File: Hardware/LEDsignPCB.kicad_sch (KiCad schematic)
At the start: 0 parts

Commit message: PD chip and usbc receptacle
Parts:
- added J?: USB_C_Receptacle, symbol Connector:USB_C_Receptacle
- added U?: CH224K, Package_SO:SSOP-10-1EP_3.9x4.9mm_P1mm_EP2.1x3.3mm, symbol Interface_USB:CH224K
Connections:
- new net: J?.A1 (GND), J?.A12 (GND), J?.B1 (GND), J?.B12 (GND)
- new net: J?.A4 (VBUS), J?.A9 (VBUS), J?.B4 (VBUS), J?.B9 (VBUS)
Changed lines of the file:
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@@
 	(generator_version "9.0")
 	(paper "A4")
+	(symbol
+		(lib_id "Connector:USB_C_Receptacle")
+		(at 50.8 60.96 0)
+		(unit 1)
+		(exclude_from_sim no)
+		(in_bom yes)
+		(on_board yes)
+		(dnp no)
+		(fields_autoplaced yes)
+		(property "Reference" "J?"
+			(at 50.8 27.94 0)
+			(effects
+				(font
+					(size 1.27 1.27)
+				)
+			)
+		)
+		(property "Value" "USB_C_Receptacle"
+			(at 50.8 30.48 0)
+			(effects
+				(font
+					(size 1.27 1.27)
+				)
+			)
+		)
+		(property "Footprint" ""
+			(at 54.61 60.96 0)
+			(effects
+				(font
+					(size 1.27 1.27)
+				)
+				(hide yes)
+			)
+		)
+		(property "Datasheet" "https://www.usb.org/sites/default/files/documents/usb_type-c.zip"
+			(at 54.61 60.96 0)
+			(effects
+				(font
+					(size 1.27 1.27)
+				)
+				(hide yes)
+			)
+		)
+		(property "Description" "USB Full-Featured Type-C Receptacle connector"
+			(at 50.8 60.96 0)
+			(effects
+				(font
+					(size 1.27 1.27)
+				)
+				(hide yes)
+			)
+		)
+		(pin "S1"
+		)
+		(pin "B2"
+		)
+		(pin "A8"
+		)
+		(pin "A10"
+		)
+		(pin "A11"
+		)
+		(pin "B3"
+		)
+		(pin "A1"
+		)
+		(pin "A12"
+		)
+		(pin "B1"
+		)
+		(pin "B12"
+		)
+		(pin "A4"
+		)
+		(pin "A9"
+		)
+		(pin "B4"
+		)
+		(pin "B9"
+		)
+		(pin "A5"
+		)
+		(pin "B5"
+		)
+		(pin "A7"
+		)
+		(pin "B7"
+		)
+		(pin "A6"
+		)
+		(pin "B6"
+		)
+		(pin "B10"
+		)
+		(pin "B11"
+		)
+		(pin "A3"
+		)
+		(pin "A2"
+		)
+		(pin "B8"
+		)
+		(instances
+			(project ""
+				(path "/bd70e714-05b6-457c-88d3-c29e19a48f7d"
+					(reference "J?")
+					(unit 1)
+				)
+			)
+		)
+	)
+	(symbol
+		(lib_id "Interface_USB:CH224K")
+		(at 128.27 63.5 0)
+		(unit 1)
+		(exclude_from_sim no)
+		(in_bom yes)
+		(on_board yes)
+		(dnp no)
+		(fields_autoplaced yes)
+		(property "Reference" "U?"
+			(at 130.4133 73.66 0)
+			(effects
+				(font
+					(size 1.27 1.27)
+				)
+				(justify left)
+			)
+		)
+		(property "Value" "CH224K"
+			(at 130.4133 76.2 0)
+			(effects
+				(font
+					(size 1.27 1.27)
+				)
+				(justify left)
+			)
+		)
+		(property "Footprint" "Package_SO:SSOP-10-1EP_3.9x4.9mm_P1mm_EP2.1x3.3mm"
+			(at 128.27 87.63 0)
+			(effects
+				(font
+					(size 1.27 1.27)
+				)
+				(hide yes)
+			)
+		)
+		(property "Datasheet" "https://www.wch.cn/downloads/file/301.html"
+			(at 128.27 49.53 0)
+			(effects
+				(font
+					(size 1.27 1.27)
+				)
+				(hide yes)
+			)
+		)
+		(property "Description" "100W USB Type-C PD3.0/2.0, BC1.2 Sink Controller, SSOP-10"
+			(at 128.27 63.5 0)
+			(effects
+				(font
+					(size 1.27 1.27)
+				)
+				(hide yes)
+			)
+		)
+		(pin "3"
+		)
+		(pin "9"
+		)
+		(pin "2"
+		)
+		(pin "4"
+		)
+		(pin "5"
+		)
+		(pin "1"
+		)
+		(pin "10"
+		)
+		(pin "7"
+		)
+		(pin "6"
+		)
+		(pin "11"
+		)
+		(pin "8"
+		)
+		(instances
+			(project ""
+				(path "/bd70e714-05b6-457c-88d3-c29e19a48f7d"
+					(reference "U?")
+					(unit 1)
+				)
+			)
+		)
+	)
 	(sheet_instances
 		(path "/"

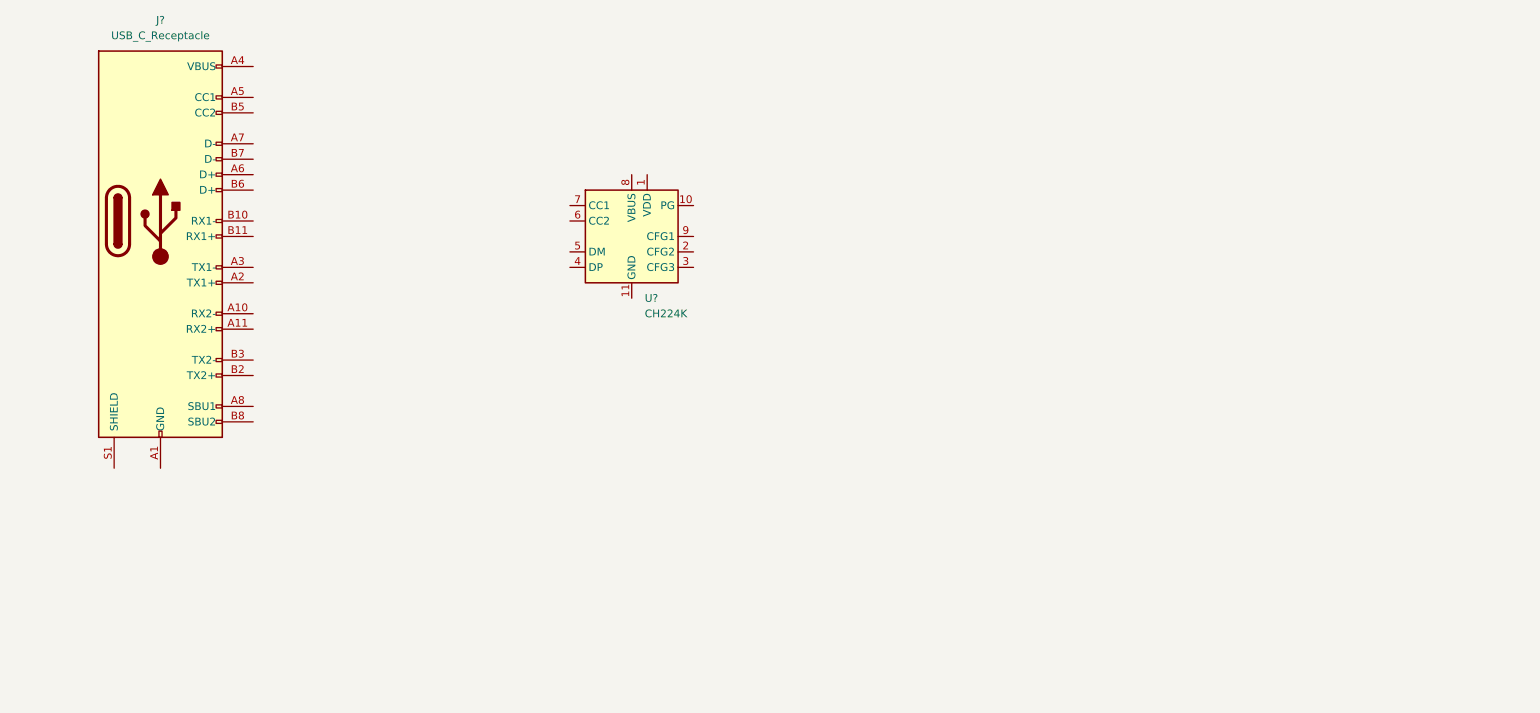
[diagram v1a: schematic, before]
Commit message: rough schematic with most components placed
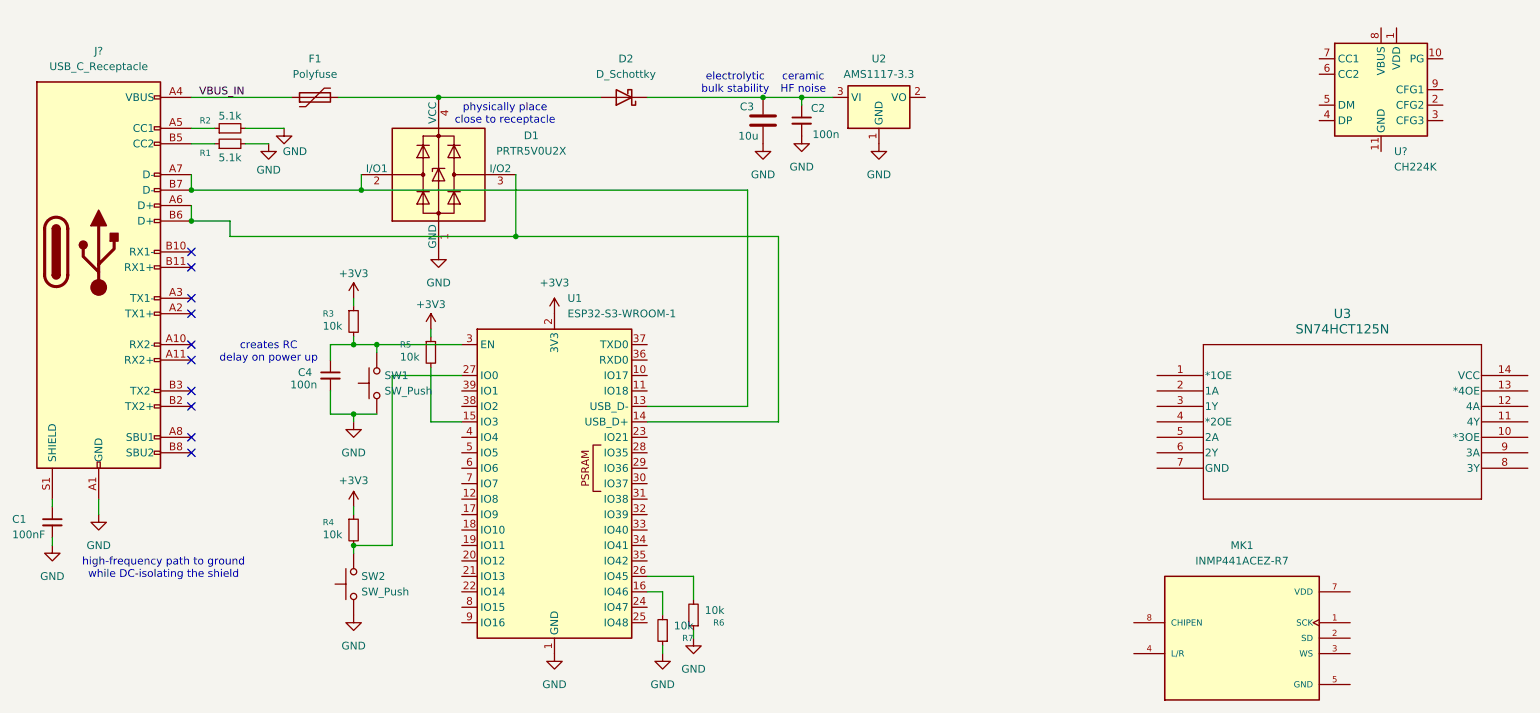
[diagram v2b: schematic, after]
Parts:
- added C1: 100nF, symbol Device:C_Small
- added C2, C4: 100n, symbol Device:C_Small
- added C3: 10u, symbol Device:C
- added D1: PRTR5V0U2X, Package_TO_SOT_SMD:SOT-143, symbol Power_Protection:PRTR5V0U2X
- added D2: D_Schottky, symbol Device:D_Schottky
- added F1: Polyfuse, Fuse:Fuse_1206_3216Metric_Pad1.42x1.75mm_HandSolder, symbol Device:Polyfuse
- added MK1: INMP441ACEZ-R7, INMP441ACEZ-R7:MIC_INMP441ACEZ-R7, symbol LED Sign:INMP441ACEZ-R7
- added R1, R2: 5.1k, symbol Device:R_Small
- added R3, R4, R5, R6, R7: 10k, symbol Device:R_Small
- added SW1, SW2: SW_Push, symbol Switch:SW_Push
- added U1: ESP32-S3-WROOM-1, RF_Module:ESP32-S3-WROOM-1, symbol RF_Module:ESP32-S3-WROOM-1
- added U2: AMS1117-3.3, Package_TO_SOT_SMD:SOT-223-3_TabPin2, symbol Regulator_Linear:AMS1117-3.3
- added U3: SN74HCT125N, N14, symbol LED Sign:SN74HCT125N
- J?: footprint (none) -> Connector_USB:USB_C_Receptacle_GCT_USB4085
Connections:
- net GND: now reaches J?.A1 (GND), J?.A12 (GND), J?.B1 (GND), J?.B12 (GND)
- net GND: now also C1.2, C2.2, C3.2, C4.2, D1.1 (GND), MK1.5 (GND), MK1.6 (GND), MK1.9 (GND), R1.2, R2.2, R6.1, R7.1, SW1.1, SW2.1, U1.1 (GND), U1.40 (GND), U1.41 (GND), U2.1 (GND)
- net VBUS_IN: now reaches J?.A4 (VBUS), J?.A9 (VBUS), J?.B4 (VBUS), J?.B9 (VBUS)
- net VBUS_IN: now also F1.1
- net at J?.A5 (CC1): now also R2.1
- net at J?.A6 (D+): now also J?.B6 (D+), D1.3 (I/O2), U1.14 (USB_D+)
- net at J?.A7 (D-): now also J?.B7 (D-), D1.2 (I/O1), U1.13 (USB_D-)
- net at J?.B5 (CC2): now also R1.1
- net at J?.S1 (SHIELD): now also C1.1
- new net: R5.2, U1.15 (IO3)
- new net: R7.2, U1.16 (IO46)
- new net: R6.2, U1.26 (IO45)
- new net: R4.2, SW2.2, U1.27 (IO0)
- new net: C4.1, R3.2, SW1.2, U1.3 (EN)
- new net: C2.1, C3.1, D2.1 (K), U2.3 (VI)
- new net: D1.4 (VCC), D2.2 (A), F1.2
- new net +3V3: R3.1, R4.1, R5.1, U1.2 (3V3)
- no-connect marks 0 -> 10
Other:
- note added: "ceramic HF noise"
- note added: "creates RC delay on power up"
- note added: "electrolytic bulk stability"
- note added: "high-frequency path to ground while DC-isolating the shield"
- note added: "physically place close to receptacle"
- moved on the sheet: J?, U?

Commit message: worked on schematic some more
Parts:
- added C5, C7, C8: 100n, symbol Device:C_Small
- added C6: 1u, symbol Device:C
- added R10: 100k, symbol Device:R
- added R11, R9: R, symbol Device:R
- added R8: 6.8k, symbol Device:R
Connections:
- net +3V3: now also U?.1 (VDD), C5.1, C6.1, C7.1, C8.1, R10.2, R11.1; no longer U1.2 (3V3)
- net GND: now also U?.11 (GND), C6.2, R8.2
- net BOOT: now reaches R4.2, SW2.2, U1.27 (IO0)
- net RESET: now reaches C4.1, R3.2, SW1.2, U1.3 (EN)
- net LED1: now reaches U1.4 (IO4)
- net LED2: now reaches U1.5 (IO5)
- net at C2.1, C3.1, U2.3 (VI): no longer D2.1 (K)
- net CC1: now reaches J?.A5 (CC1), R2.1
- net CC1: now also U?.7 (CC1)
- net CC2: now reaches J?.B5 (CC2), R1.1
- net CC2: now also U?.6 (CC2)
- net at U?.10 (PG): now also R10.1
- net at U?.4 (DP): now also U?.5 (DM)
- net at U?.8 (VBUS): now also R11.2, R9.2
- net at U?.9 (CFG1): now also R8.1
- new net: C5.2, C7.2, C8.2, U1.2 (3V3)
- new net: D2.1 (K), R9.1
- no-connect marks 10 -> 12
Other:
- note added: "as close to pin as possible"
- moved on the sheet: C2, C3, R1, R2, U2, U?

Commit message: added 3D models, symbols, footprints, finished buck circuit
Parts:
- added C10, C13, C14: 100n, symbol Device:C_Small
- added C11, C12: 47u, symbol Device:C
- added C15: 8.2n, symbol Device:C
- added C16: 20p, symbol Device:C_Small
- added C17: 1n, symbol Device:C_Small
- added C9: 22u, symbol Device:C
- added D3: SS34, Diode_SMD:D_SMA, symbol Diode:SS34
- added L1: 2.5u, symbol Device:L
- added R12: 100k, symbol Device:R
- added R13: 10.2k, symbol Device:R
- added R14: 1.96k, symbol Device:R
- added R15: 69.8k, symbol Device:R
- added U4: TPS54332DDA, DDA8_3X2P13, symbol LED Sign:TPS54332DDA
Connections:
- net +3V3: now also U2.2 (VO), R12.1
- net BOOT: now also C14.2, U4.1 (BOOT)
- net GND: now also C10.2, C11.2, C12.2, C13.2, C15.2, C16.2, C17.2, C9.2, D3.1 (K), L1.1, R14.2, U4.7 (GND)
- net +5V: now reaches C2.1, C3.1, U2.3 (VI)
- net +5V: now also C11.1, C12.1, C13.1, L1.2, R13.1
- net PG: now reaches R10.1, U?.10 (PG)
- net PG: now also R12.2, U4.3 (EN)
- new net: C15.1, U4.4 (SS)
- new net: R13.2, R14.1, U4.5 (VSENSE)
- new net: C17.1, R15.2
- new net +9V: C10.1, C9.1, U4.2 (VIN)
- new net COMP: C16.1, R15.1, U4.6 (COMP)
- new net SW: C14.1, D3.2 (A), U4.8 (PH)
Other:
- note added: "Vout = Vref × (1 + Rfbt/Rfbb) Vout = 0.8 × (1 + 10.2k/1.96k) Vout = 0.8 × (1 + 5.204) Vout = 0.8 × 6.204 = 4.96V ≈ 5V ✅ use E96 resistors"
- note added: "ceramic"
- note added: "ceramic X7R"
- note added: "ceramic X7R 16V+ rated"
- note added: "choose X7R voltage rating at least 2x 3x higher"
- note added: "place close to SW pin as possible short trace to GND 450mV, 3A Schottky diode"
- note added: "place close to VIN pin"
- note added: "saturation current rating >= 4.5A use shielded inductor"
- note added: "use at least 10V rated caps"
- moved on the sheet: MK1, U3

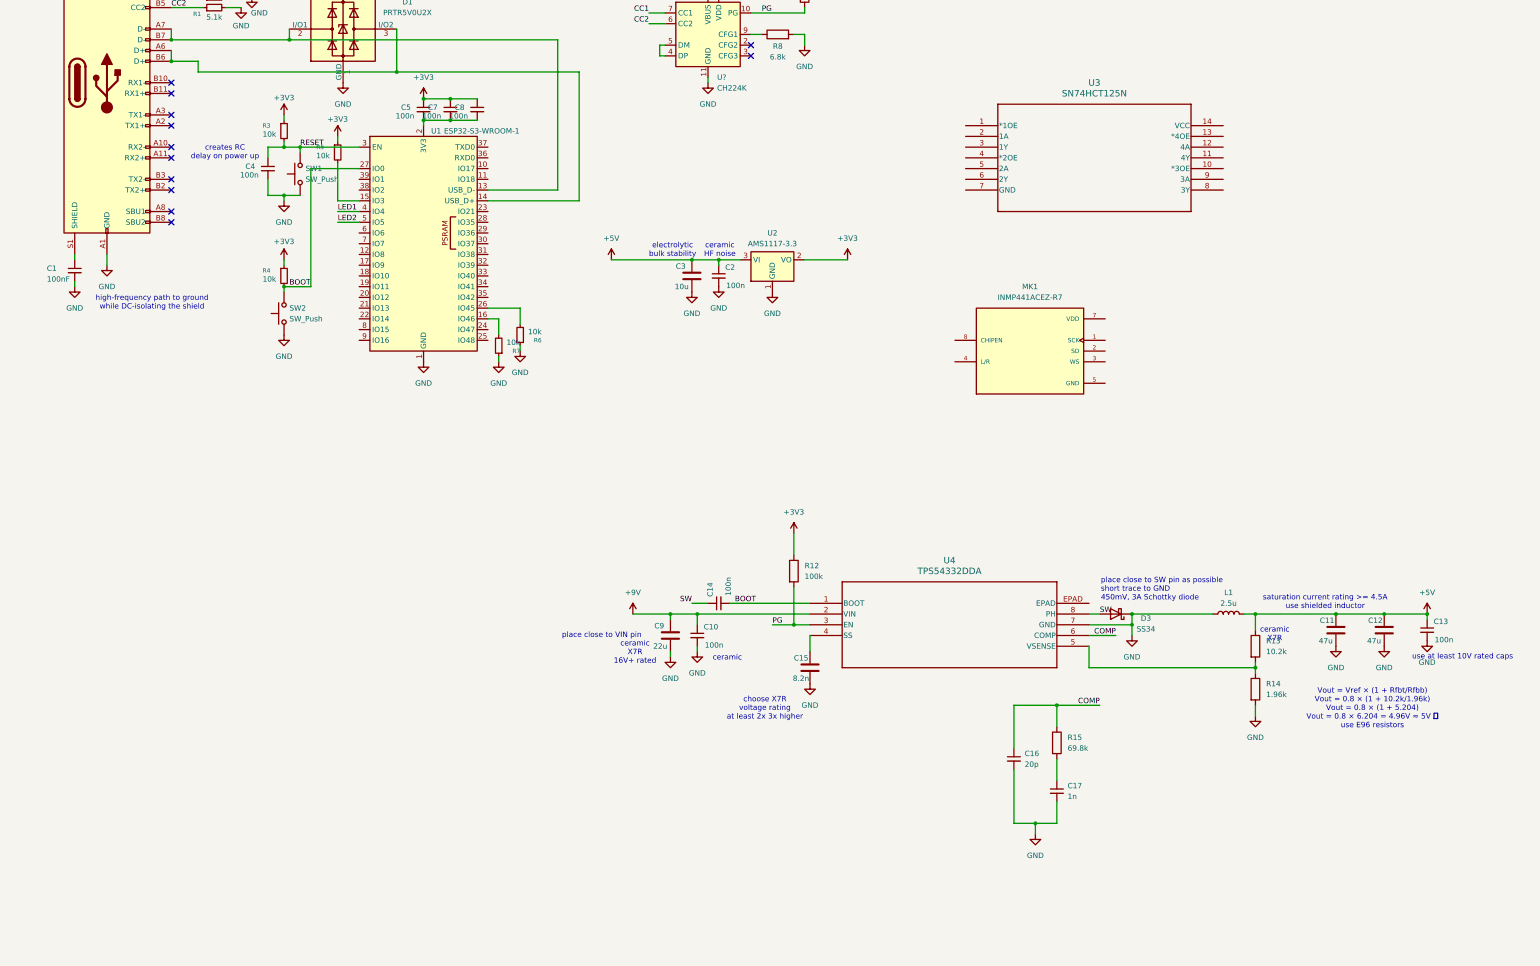
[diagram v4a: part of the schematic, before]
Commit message: changed microphone
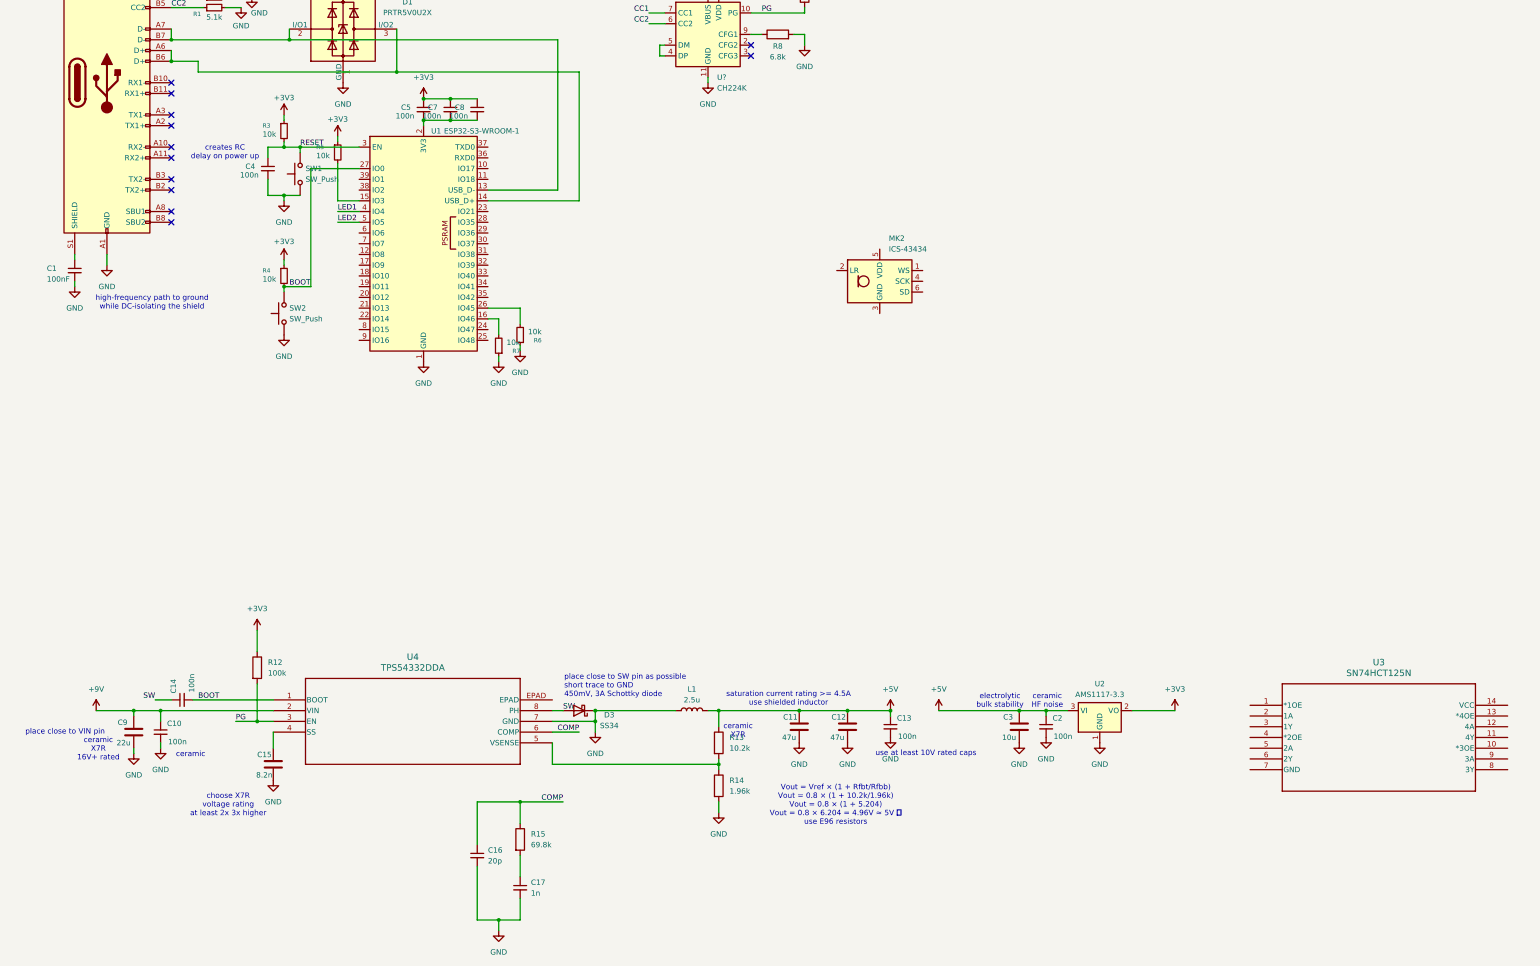
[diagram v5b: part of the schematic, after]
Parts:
- removed MK1: INMP441ACEZ-R7, INMP441ACEZ-R7:MIC_INMP441ACEZ-R7, symbol LED Sign:INMP441ACEZ-R7
- added MK2: ICS-43434, Sensor_Audio:InvenSense_ICS-43434-6_3.5x2.65mm, symbol Sensor_Audio:ICS-43434
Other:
- moved on the sheet: C10, C11, C12, C13, C14, C15, C16, C17, C2, C3, C9, D3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
